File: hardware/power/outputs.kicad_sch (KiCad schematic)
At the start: 9 parts, among them J401 MASTER, J402 CHAIN 1, J403 CHAIN 2

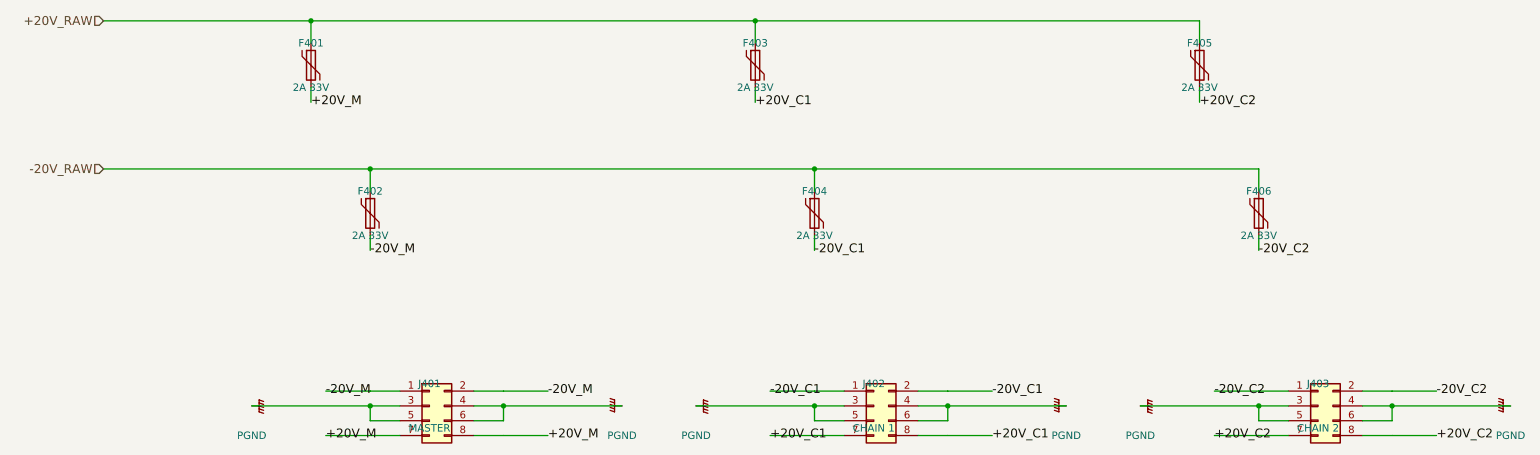
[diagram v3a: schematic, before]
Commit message: Power board: PCB placed and routed by scripts, panel-mount brick jack, small module without chain 2 (decisions 182, 185, 186)
Co-Authored-By: Claude Opus 5.5 <noreply@anthropic.com>
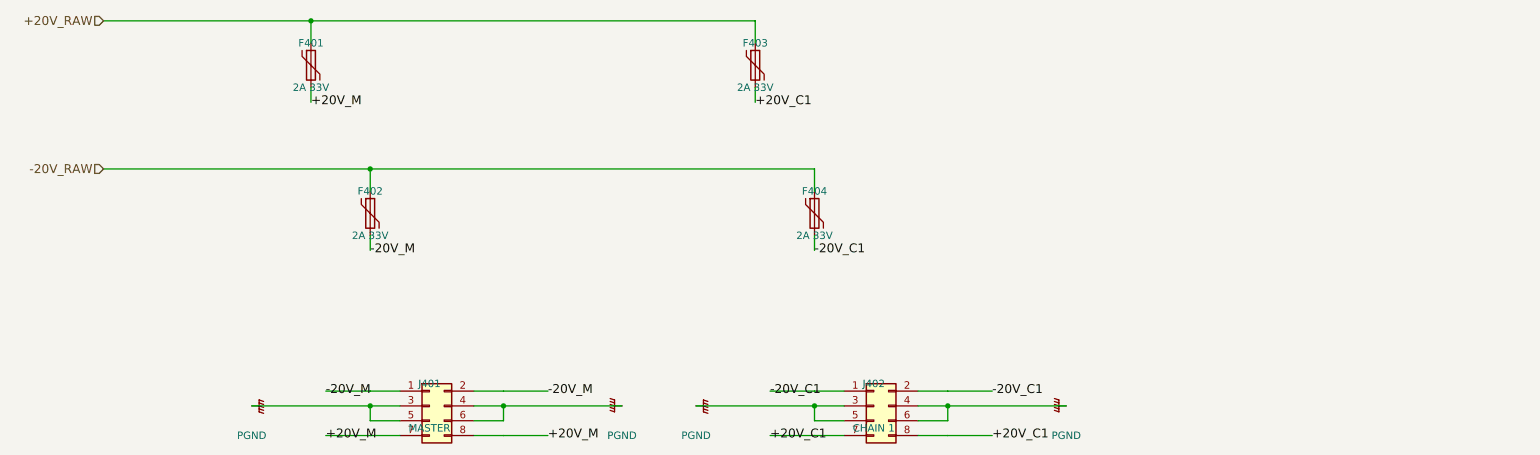
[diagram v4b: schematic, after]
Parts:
- removed F405, F406: 2A 33V, Fuse:Fuse_1812_4532Metric, symbol Device:Polyfuse
- removed J403: CHAIN 2, Connector_IDC:IDC-Header_2x04_P2.54mm_Vertical, symbol Connector_Generic:Conn_02x04_Odd_Even
